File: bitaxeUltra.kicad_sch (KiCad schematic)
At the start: 8 parts, among them J3 Barrel_Jack_Switch

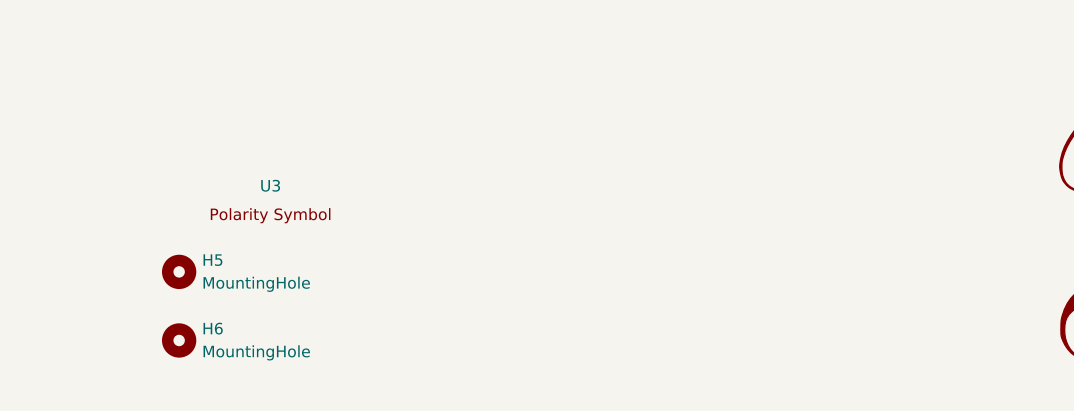
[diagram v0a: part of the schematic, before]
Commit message: revised heat-sinking. Supports heatsinks with 40x40 size with holes 35x35, 32x32 and 33x33
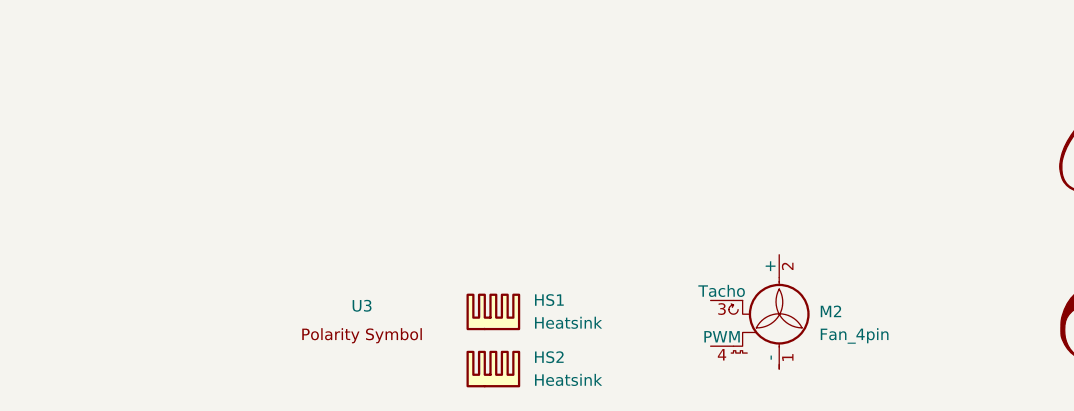
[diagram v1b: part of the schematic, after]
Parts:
- removed H5, H6: MountingHole, MountingHole:MountingHole_3.5mm, symbol Mechanical:MountingHole
- added HS1, HS2: Heatsink, symbol Mechanical:Heatsink
- added M2: Fan_4pin, symbol Motor:Fan_4pin
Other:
- moved on the sheet: U3
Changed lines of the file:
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@@
     )
   )
-  (symbol (lib_id "Mechanical:MountingHole") (at 63.5 186.055 0) (unit 1)
-    (in_bom no) (on_board yes) (dnp no) (fields_autoplaced)
-    (property "Reference" "H6" (at 66.04 184.7849 0)
-      (effects (font (size 1.27 1.27)) (justify left))
-    )
-    (property "Value" "MountingHole" (at 66.04 187.3249 0)
-      (effects (font (size 1.27 1.27)) (justify left))
-    )
-    (property "Footprint" "MountingHole:MountingHole_3.5mm" (at 63.5 186.055 0)
-      (effects (font (size 1.27 1.27)) hide)
-    )
-    (property "Datasheet" "~" (at 63.5 186.055 0)
-      (effects (font (size 1.27 1.27)) hide)
-    )
-    (property "Distributor" "-" (at 63.5 186.055 0)
-      (effects (font (size 1.27 1.27)) hide)
-    )
-    (instances
-      (project "bitaxeUltra"
-        (path "/e63e39d7-6ac0-4ffd-8aa3-1841a4541b55"
-          (reference "H6") (unit 1)
+  (symbol (lib_id "Motor:Fan_4pin") (at 130.175 184.15 0) (unit 1)
+    (in_bom yes) (on_board no) (dnp no) (fields_autoplaced)
+    (property "Reference" "M2" (at 134.62 182.88 0)
+      (effects (font (size 1.27 1.27)) (justify left))
+    )
+    (property "Value" "Fan_4pin" (at 134.62 185.42 0)
+      (effects (font (size 1.27 1.27)) (justify left))
+    )
+    (property "Footprint" "" (at 130.175 183.896 0)
+      (effects (font (size 1.27 1.27)) hide)
+    )
+    (property "Datasheet" "http://www.formfactors.org/developer%5Cspecs%5Crev1_2_public.pdf" (at 130.175 183.896 0)
+      (effects (font (size 1.27 1.27)) hide)
+    )
+    (property "Distributor" "X" (at 130.175 184.15 0)
+      (effects (font (size 1.27 1.27)) hide)
+    )
+    (property "Manufacturer" " Noctua NF-A4x10 5V" (at 130.175 184.15 0)
+      (effects (font (size 1.27 1.27)) hide)
+    )
+    (pin "1")
+    (pin "2")
+    (pin "3")
+    (pin "4")
+    (instances
+      (project "bitaxeUltra"
+        (path "/e63e39d7-6ac0-4ffd-8aa3-1841a4541b55"
+          (reference "M2") (unit 1)
         )
       )
@@
     )
   )
-  (symbol (lib_id "Mechanical:MountingHole") (at 63.5 178.435 0) (unit 1)
-    (in_bom no) (on_board yes) (dnp no) (fields_autoplaced)
-    (property "Reference" "H5" (at 66.04 177.1649 0)
-      (effects (font (size 1.27 1.27)) (justify left))
-    )
-    (property "Value" "MountingHole" (at 66.04 179.7049 0)
-      (effects (font (size 1.27 1.27)) (justify left))
-    )
-    (property "Footprint" "MountingHole:MountingHole_3.5mm" (at 63.5 178.435 0)
-      (effects (font (size 1.27 1.27)) hide)
-    )
-    (property "Datasheet" "~" (at 63.5 178.435 0)
-      (effects (font (size 1.27 1.27)) hide)
-    )
-    (property "Distributor" "-" (at 63.5 178.435 0)
-      (effects (font (size 1.27 1.27)) hide)
-    )
-    (instances
-      (project "bitaxeUltra"
-        (path "/e63e39d7-6ac0-4ffd-8aa3-1841a4541b55"
-          (reference "H5") (unit 1)
-        )
-      )
-    )
-  )
   (symbol (lib_id "power:+12V") (at 63.5 48.26 0) (unit 1)
     (in_bom yes) (on_board yes) (dnp no) (fields_autoplaced)
@@
     )
   )
-  (symbol (lib_id "bitaxe:polarity") (at 74.93 170.815 0) (unit 1)
+  (symbol (lib_id "Mechanical:Heatsink") (at 98.425 191.135 0) (unit 1)
+    (in_bom yes) (on_board no) (dnp no) (fields_autoplaced)
+    (property "Reference" "HS2" (at 102.87 187.96 0)
+      (effects (font (size 1.27 1.27)) (justify left))
+    )
+    (property "Value" "Heatsink" (at 102.87 190.5 0)
+      (effects (font (size 1.27 1.27)) (justify left))
+    )
+    (property "Footprint" "" (at 98.7298 191.135 0)
+      (effects (font (size 1.27 1.27)) hide)
+    )
+    (property "Datasheet" "~" (at 98.7298 191.135 0)
+      (effects (font (size 1.27 1.27)) hide)
+    )
+    (property "Distributor" "D" (at 98.425 191.135 0)
+      (effects (font (size 1.27 1.27)) hide)
+    )
+    (property "Manufacturer" "ATS-FPX040040025-94-C2-R0" (at 98.425 191.135 0)
+      (effects (font (size 1.27 1.27)) hide)
+    )
+    (property "OrderNr" "ATS1674-ND" (at 98.425 191.135 0)
+      (effects (font (size 1.27 1.27)) hide)
+    )
+    (instances
+      (project "bitaxeUltra"
+        (path "/e63e39d7-6ac0-4ffd-8aa3-1841a4541b55"
+          (reference "HS2") (unit 1)
+        )
+      )
+    )
+  )
+  (symbol (lib_id "bitaxe:polarity") (at 85.09 184.15 0) (unit 1)
     (in_bom no) (on_board yes) (dnp no) (fields_autoplaced)
-    (property "Reference" "U3" (at 73.66 168.91 0)
-      (effects (font (size 1.27 1.27)))
-    )
-    (property "Value" "~" (at 74.93 170.815 0)
-      (effects (font (size 1.27 1.27)))
-    )
-    (property "Footprint" "bitaxe:polarity" (at 74.93 170.815 0)
-      (effects (font (size 1.27 1.27)) hide)
-    )
-    (property "Datasheet" "" (at 74.93 170.815 0)
-      (effects (font (size 1.27 1.27)) hide)
-    )
-    (property "Distributor" "-" (at 74.93 170.815 0)
+    (property "Reference" "U3" (at 83.82 182.245 0)
+      (effects (font (size 1.27 1.27)))
+    )
+    (property "Value" "~" (at 85.09 184.15 0)
+      (effects (font (size 1.27 1.27)))
+    )
+    (property "Footprint" "bitaxe:polarity" (at 85.09 184.15 0)
+      (effects (font (size 1.27 1.27)) hide)
+    )
+    (property "Datasheet" "" (at 85.09 184.15 0)
+      (effects (font (size 1.27 1.27)) hide)
+    )
+    (property "Distributor" "-" (at 85.09 184.15 0)
       (effects (font (size 1.27 1.27)) hide)
     )
@@
         )
       )
+    )
+  )
+  (symbol (lib_id "Mechanical:Heatsink") (at 98.425 184.785 0) (unit 1)
+    (in_bom yes) (on_board no) (dnp no) (fields_autoplaced)
+    (property "Reference" "HS1" (at 102.87 181.61 0)
+      (effects (font (size 1.27 1.27)) (justify left))
+    )
+    (property "Value" "Heatsink" (at 102.87 184.15 0)
+      (effects (font (size 1.27 1.27)) (justify left))
+    )
+    (property "Footprint" "" (at 98.7298 184.785 0)
+      (effects (font (size 1.27 1.27)) hide)
+    )
+    (property "Datasheet" "~" (at 98.7298 184.785 0)
+      (effects (font (size 1.27 1.27)) hide)
+    )
+    (property "Distributor" "D" (at 98.425 184.785 0)
+      (effects (font (size 1.27 1.27)) hide)
+    )
+    (property "Manufacturer" "ATS-CPX040040025-184-C1-R0" (at 98.425 184.785 0)
+      (effects (font (size 1.27 1.27)) hide)
+    )
+    (property "OrderNr" "ATS35997-ND" (at 98.425 184.785 0)
+      (effects (font (size 1.27 1.27)) hide)
+    )
+    (instances
+      (project "bitaxeUltra"
+        (path "/e63e39d7-6ac0-4ffd-8aa3-1841a4541b55"
+          (reference "HS1") (unit 1)
+        )
+      )

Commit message: added gerbers and bom
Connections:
- no-connect marks 0 -> 4
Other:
- sheet BM1366 ports: added none; removed 3V3
- sheet Pi ports: added none; removed +3V3
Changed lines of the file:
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@@
   (junction (at 63.5 52.07) (diameter 0) (color 0 0 0 0)
   )
-  (wire (pts (xy 100.33 102.87) (xy 121.285 102.87))
-    (stroke (width 0) (type default))
-  )
+  (no_connect (at 130.175 176.53))
+  (no_connect (at 130.175 189.23))
+  (no_connect (at 122.555 186.69))
+  (no_connect (at 122.555 181.61))
   (wire (pts (xy 63.5 66.675) (xy 63.5 66.04))
     (stroke (width 0) (type default))
@@
     (stroke (width 0) (type default))
   )
-  (wire (pts (xy 63.5 52.07) (xy 83.185 52.07))
-    (stroke (width 0) (type default))
-  )
   (wire (pts (xy 131.445 82.55) (xy 144.78 82.55))
     (stroke (width 0) (type default))
@@
     (stroke (width 0) (type default))
   )
-  (wire (pts (xy 78.105 77.47) (xy 78.105 92.71))
-    (stroke (width 0) (type default))
-  )
   (wire (pts (xy 75.565 87.63) (xy 82.55 87.63))
     (stroke (width 0) (type default))
@@
     (stroke (width 0) (type default))
   )
+  (wire (pts (xy 63.5 52.07) (xy 82.55 52.07))
+    (stroke (width 0) (type default))
+  )
   (wire (pts (xy 55.245 54.61) (xy 55.245 52.07))
     (stroke (width 0) (type default))
@@
     (stroke (width 0) (type default))
   )
-  (wire (pts (xy 100.33 105.41) (xy 118.745 105.41))
-    (stroke (width 0) (type default))
-  )
   (wire (pts (xy 76.835 90.17) (xy 82.55 90.17))
     (stroke (width 0) (type default))
@@
     (stroke (width 0) (type default))
   )
-  (wire (pts (xy 78.105 92.71) (xy 82.55 92.71))
-    (stroke (width 0) (type default))
-  )
   (wire (pts (xy 43.815 54.61) (xy 43.815 57.15))
     (stroke (width 0) (type default))
@@
     (stroke (width 0) (type default))
   )
-  (wire (pts (xy 144.78 77.47) (xy 78.105 77.47))
-    (stroke (width 0) (type default))
-  )
-  (wire (pts (xy 100.457 52.07) (xy 110.49 52.07))
+  (wire (pts (xy 99.695 52.07) (xy 110.49 52.07))
     (stroke (width 0) (type default))
   )
@@
     (stroke (width 0) (type default))
   )
-  (wire (pts (xy 100.457 64.135) (xy 132.715 64.135))
+  (wire (pts (xy 99.695 64.135) (xy 132.715 64.135))
     (stroke (width 0) (type default))
   )
@@
     (stroke (width 0) (type default))
   )
-  (wire (pts (xy 100.457 66.04) (xy 131.445 66.04))
+  (wire (pts (xy 99.695 66.04) (xy 131.445 66.04))
     (stroke (width 0) (type default))
   )
@@
     (effects (font (size 5 5) (thickness 1) bold italic) (justify left bottom))
   )
-  (label "TEMP_N" (at 102.87 105.41 0) (fields_autoplaced)
-    (effects (font (size 1.27 1.27)) (justify left bottom))
-  )
-  (label "TEMP_P" (at 102.87 102.87 0) (fields_autoplaced)
-    (effects (font (size 1.27 1.27)) (justify left bottom))
+  (symbol (lib_id "power:+3V3") (at 55.245 182.88 180) (unit 1)
+    (in_bom yes) (on_board yes) (dnp no) (fields_autoplaced)
+    (property "Reference" "#PWR095" (at 55.245 179.07 0)
+      (effects (font (size 1.27 1.27)) hide)
+    )
+    (property "Value" "+3V3" (at 55.245 187.96 0)
+      (effects (font (size 1.27 1.27)))
+    )
+    (property "Footprint" "" (at 55.245 182.88 0)
+      (effects (font (size 1.27 1.27)) hide)
+    )
+    (property "Datasheet" "" (at 55.245 182.88 0)
+      (effects (font (size 1.27 1.27)) hide)
+    )
+    (pin "1")
+    (instances
+      (project "bitaxeUltra"
+        (path "/e63e39d7-6ac0-4ffd-8aa3-1841a4541b55"
+          (reference "#PWR095") (unit 1)
+        )
+      )
+    )
+  )
+  (symbol (lib_id "power:+5V") (at 43.18 182.88 180) (unit 1)
+    (in_bom yes) (on_board yes) (dnp no) (fields_autoplaced)
+    (property "Reference" "#PWR021" (at 43.18 179.07 0)
+      (effects (font (size 1.27 1.27)) hide)
+    )
+    (property "Value" "+5V" (at 43.18 187.96 0)
+      (effects (font (size 1.27 1.27)))
+    )
+    (property "Footprint" "" (at 43.18 182.88 0)
+      (effects (font (size 1.27 1.27)) hide)
+    )
+    (property "Datasheet" "" (at 43.18 182.88 0)
+      (effects (font (size 1.27 1.27)) hide)
+    )
+    (pin "1")
+    (instances
+      (project "bitaxeUltra"
+        (path "/e63e39d7-6ac0-4ffd-8aa3-1841a4541b55"
+          (reference "#PWR021") (unit 1)
+        )
+      )
+    )
   )
   (symbol (lib_id "power:GND") (at 55.245 66.675 0) (unit 1)
@@
     )
   )
+  (symbol (lib_id "power:PWR_FLAG") (at 43.18 182.88 0) (unit 1)
+    (in_bom yes) (on_board yes) (dnp no) (fields_autoplaced)
+    (property "Reference" "#FLG02" (at 43.18 180.975 0)
+      (effects (font (size 1.27 1.27)) hide)
+    )
+    (property "Value" "PWR_FLAG" (at 43.18 178.435 0)
+      (effects (font (size 1.27 1.27)))
+    )
+    (property "Footprint" "" (at 43.18 182.88 0)
+      (effects (font (size 1.27 1.27)) hide)
+    )
+    (property "Datasheet" "~" (at 43.18 182.88 0)
+      (effects (font (size 1.27 1.27)) hide)
+    )
+    (pin "1")
+    (instances
+      (project "bitaxeUltra"
+        (path "/e63e39d7-6ac0-4ffd-8aa3-1841a4541b55"
+          (reference "#FLG02") (unit 1)
+        )
+      )
+    )
+  )
   (symbol (lib_id "power:GND") (at 63.5 66.675 0) (unit 1)
     (in_bom yes) (on_board yes) (dnp no)
@@
         (path "/e63e39d7-6ac0-4ffd-8aa3-1841a4541b55"
           (reference "#PWR09") (unit 1)
+        )
+      )
+    )
+  )
+  (symbol (lib_id "power:+12V") (at 32.385 182.88 180) (unit 1)
+    (in_bom yes) (on_board yes) (dnp no) (fields_autoplaced)
+    (property "Reference" "#PWR093" (at 32.385 179.07 0)
+      (effects (font (size 1.27 1.27)) hide)
+    )
+    (property "Value" "+12V" (at 32.385 187.96 0)
+      (effects (font (size 1.27 1.27)))
+    )
+    (property "Footprint" "" (at 32.385 182.88 0)
+      (effects (font (size 1.27 1.27)) hide)
+    )
+    (property "Datasheet" "" (at 32.385 182.88 0)
+      (effects (font (size 1.27 1.27)) hide)
+    )
+    (pin "1")
+    (instances
+      (project "bitaxeUltra"
+        (path "/e63e39d7-6ac0-4ffd-8aa3-1841a4541b55"
+          (reference "#PWR093") (unit 1)
+        )
+      )
+    )
+  )
+  (symbol (lib_id "power:PWR_FLAG") (at 32.385 182.88 0) (unit 1)
+    (in_bom yes) (on_board yes) (dnp no)
+    (property "Reference" "#FLG01" (at 32.385 180.975 0)
+      (effects (font (size 1.27 1.27)) hide)
+    )
+    (property "Value" "PWR_FLAG" (at 32.385 178.435 0)
+      (effects (font (size 1.27 1.27)))
+    )
+    (property "Footprint" "" (at 32.385 182.88 0)
+      (effects (font (size 1.27 1.27)) hide)
+    )
+    (property "Datasheet" "~" (at 32.385 182.88 0)
+      (effects (font (size 1.27 1.27)) hide)
+    )
+    (pin "1")
+    (instances
+      (project "bitaxeUltra"
+        (path "/e63e39d7-6ac0-4ffd-8aa3-1841a4541b55"
+          (reference "#FLG01") (unit 1)
+        )
+      )
+    )
+  )
+  (symbol (lib_id "power:PWR_FLAG") (at 55.245 182.88 0) (unit 1)
+    (in_bom yes) (on_board yes) (dnp no) (fields_autoplaced)
+    (property "Reference" "#FLG03" (at 55.245 180.975 0)
+      (effects (font (size 1.27 1.27)) hide)
+    )
+    (property "Value" "PWR_FLAG" (at 55.245 178.435 0)
+      (effects (font (size 1.27 1.27)))
+    )
+    (property "Footprint" "" (at 55.245 182.88 0)
+      (effects (font (size 1.27 1.27)) hide)
+    )
+    (property "Datasheet" "~" (at 55.245 182.88 0)
+      (effects (font (size 1.27 1.27)) hide)
+    )
+    (pin "1")
+    (instances
+      (project "bitaxeUltra"
+        (path "/e63e39d7-6ac0-4ffd-8aa3-1841a4541b55"
+          (reference "#FLG03") (unit 1)
         )
       )
@@
       (effects (font (size 1.27 1.27)) (justify right))
     )
-    (pin "3V3" input (at 82.55 92.71 180)
-      (effects (font (size 1.27 1.27)) (justify left))
-    )
     (pin "5V" input (at 82.55 90.17 180)
       (effects (font (size 1.27 1.27)) (justify left))
@@
     )
   )
-  (sheet (at 83.185 49.276) (size 17.272 19.05) (fields_autoplaced)
+  (sheet (at 82.55 49.276) (size 17.145 19.05) (fields_autoplaced)
     (stroke (width 0.1524) (type solid))
     (fill (color 255 255 194 1.0000))
-    (property "Sheetname" "Power" (at 83.185 48.5644 0)
+    (property "Sheetname" "Power" (at 82.55 48.5644 0)
       (effects (font (size 1.27 1.27)) (justify left bottom))
     )
-    (property "Sheetfile" "power.kicad_sch" (at 83.185 68.9106 0)
+    (property "Sheetfile" "power.kicad_sch" (at 82.55 68.9106 0)
       (effects (font (size 1.27 1.27)) (justify left top))
     )
-    (pin "PGOOD" output (at 100.457 66.04 0)
+    (pin "PGOOD" output (at 99.695 66.04 0)
       (effects (font (size 1.27 1.27)) (justify right))
     )
-    (pin "+1V5" output (at 100.457 52.07 0)
+    (pin "+1V5" output (at 99.695 52.07 0)
       (effects (font (size 1.27 1.27)) (justify right))
     )
-    (pin "SDN" passive (at 100.457 64.135 0)
+    (pin "SDN" passive (at 99.695 64.135 0)
       (effects (font (size 1.27 1.27)) (justify right))
     )
-    (pin "VIn" input (at 83.185 52.07 180)
+    (pin "VIn" input (at 82.55 52.07 180)
       (effects (font (size 1.27 1.27)) (justify left))
     )
@@
       (effects (font (size 1.27 1.27)) (justify left top))
     )
-    (pin "+3V3" passive (at 144.78 77.47 180)
-      (effects (font (size 1.27 1.27)) (justify left))
-    )
     (pin "+5V" passive (at 144.78 75.565 180)
